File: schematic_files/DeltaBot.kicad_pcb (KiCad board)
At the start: 2 copper layers, 241.5 x 110.5 mm, 24 parts, among them J1 USB C PD Modulle, J2 LIDAR, J3 MOTOR_L, J4 MOTOR_R, SW1 SW_SPDT, U1 Radxa_ROCK5B, U2 Buck Converter

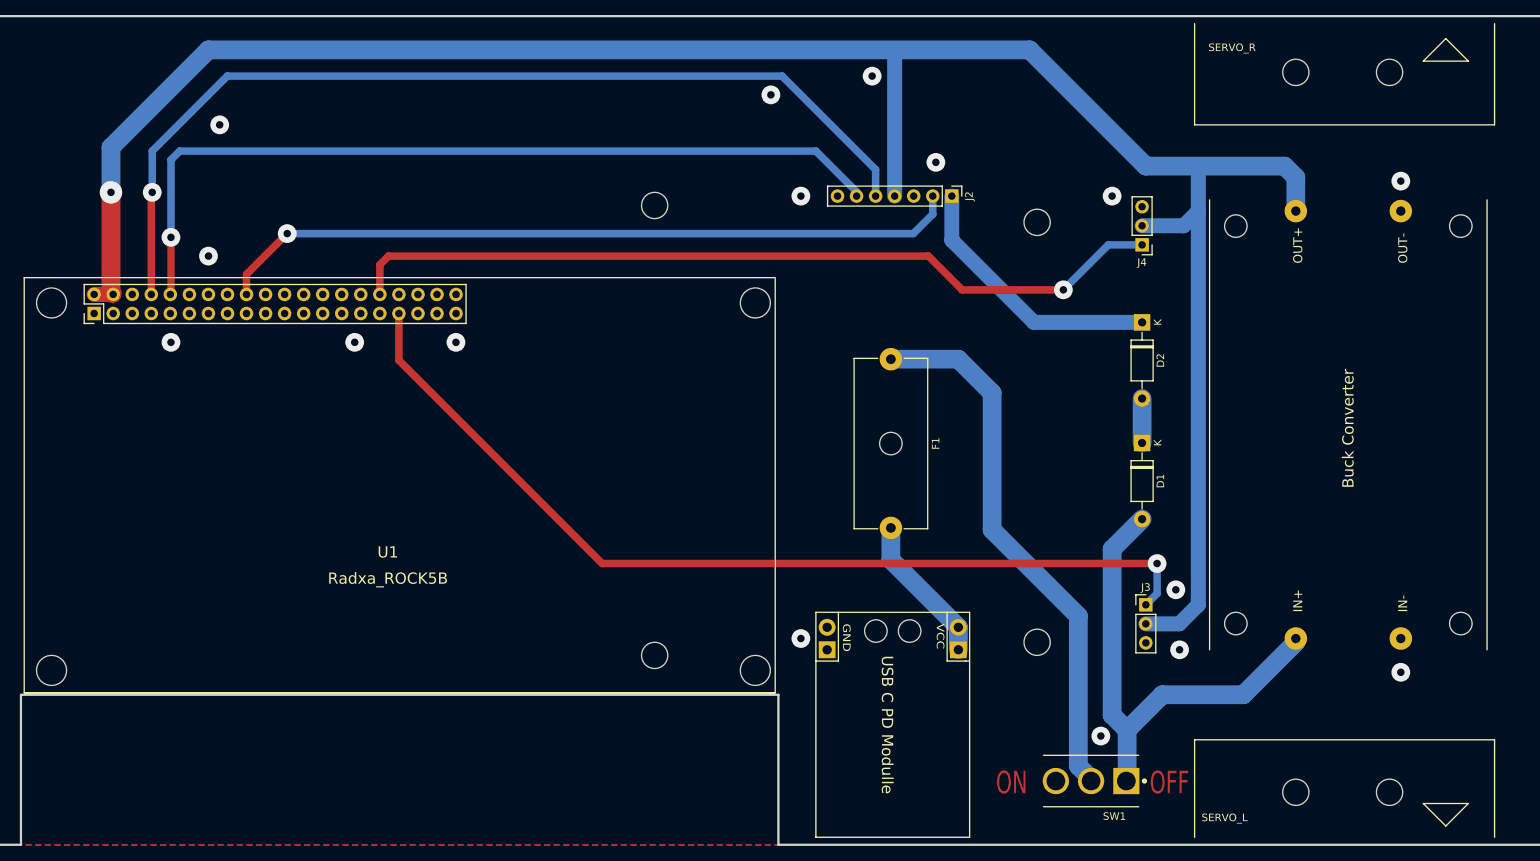
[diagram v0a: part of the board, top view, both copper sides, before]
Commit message: Schematic minor fixes
rearranged silkscreen, added capacitors to the pcb
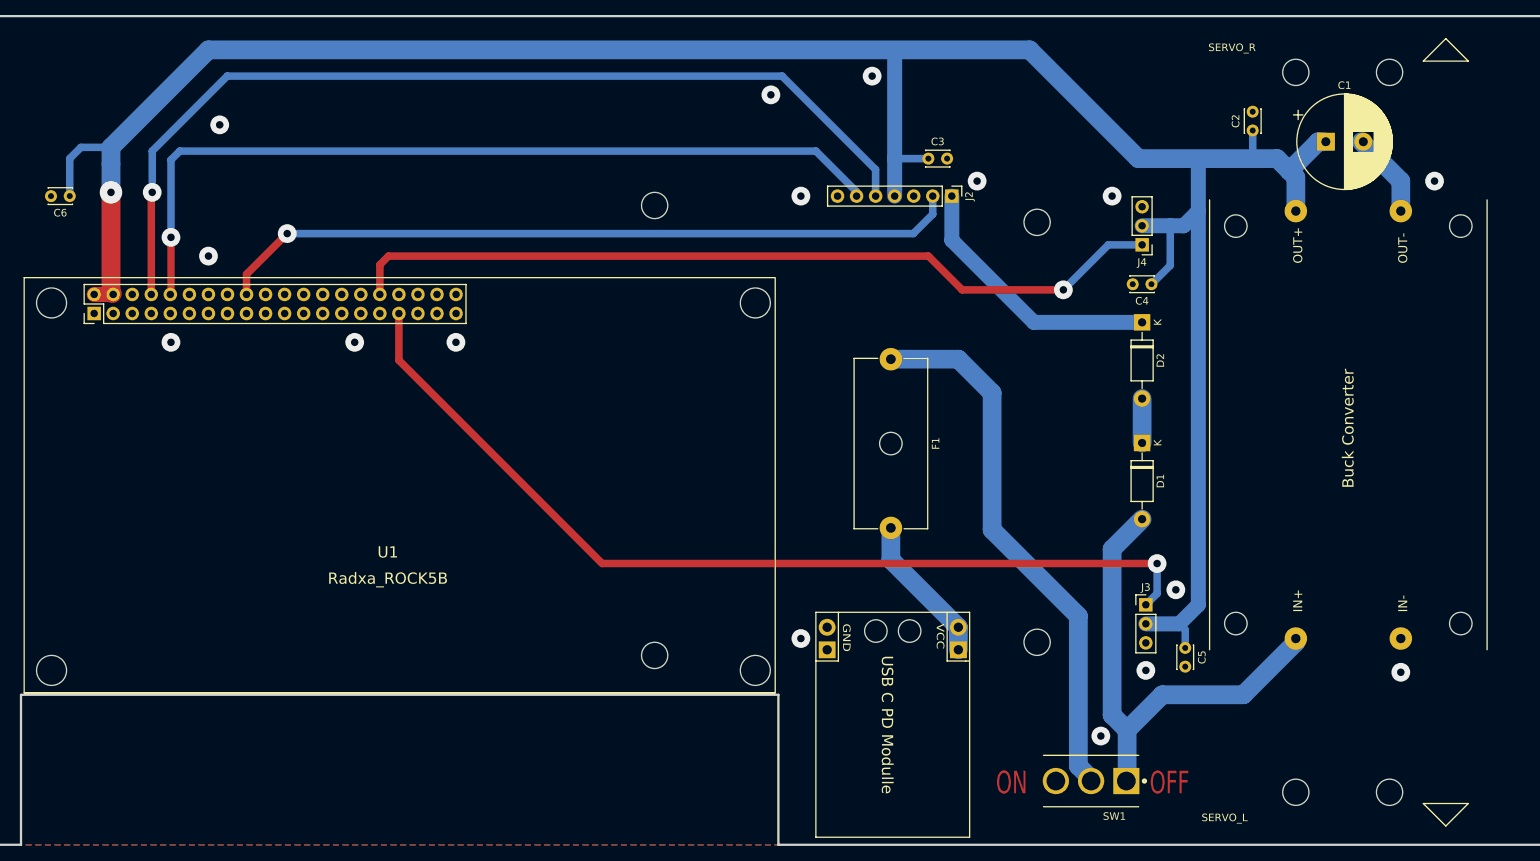
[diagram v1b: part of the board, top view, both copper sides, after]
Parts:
- added C1: 2200uF, deltabot:CP_Radial_D12.5mm_P5.00mm, F.Cu at (226.0, 52.8)
- added C2: 1uF, deltabot:C_Disc_D3.0mm_W2.0mm_P2.50mm, F.Cu at (216.2, 51.2)
- added C3: 1uF, deltabot:C_Disc_D3.0mm_W2.0mm_P2.50mm, F.Cu at (173.0, 55.0)
- added C4: 1uF, deltabot:C_Disc_D3.0mm_W2.0mm_P2.50mm, F.Cu at (202.8, 71.8)
- added C5: 1uF, deltabot:C_Disc_D3.0mm_W2.0mm_P2.50mm, F.Cu at (207.2, 120.2)
- added C6: 1uF, deltabot:C_Disc_D3.0mm_W2.0mm_P2.50mm, F.Cu at (58.5, 60.0)
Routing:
- net +5V: track 290.9 -> 329.1 mm
- net GND: track 0.00 -> 11.4 mm
